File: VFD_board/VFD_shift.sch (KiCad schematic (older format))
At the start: 2 parts

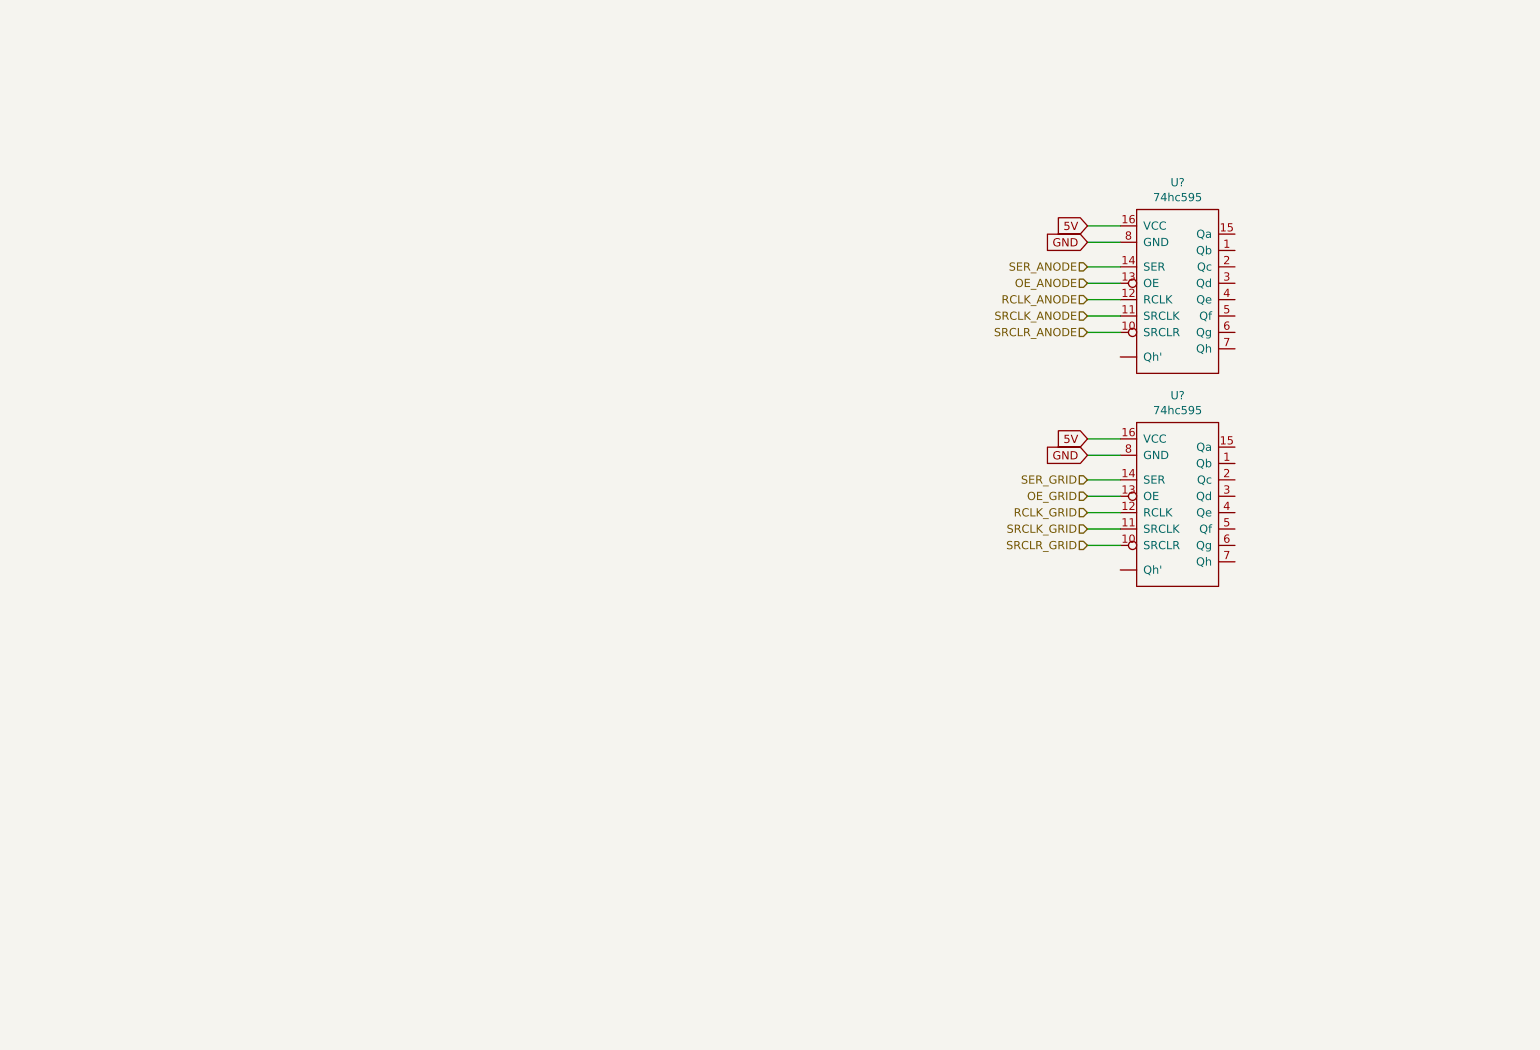
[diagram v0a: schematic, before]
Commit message: Started schematic for shift registers/drivers
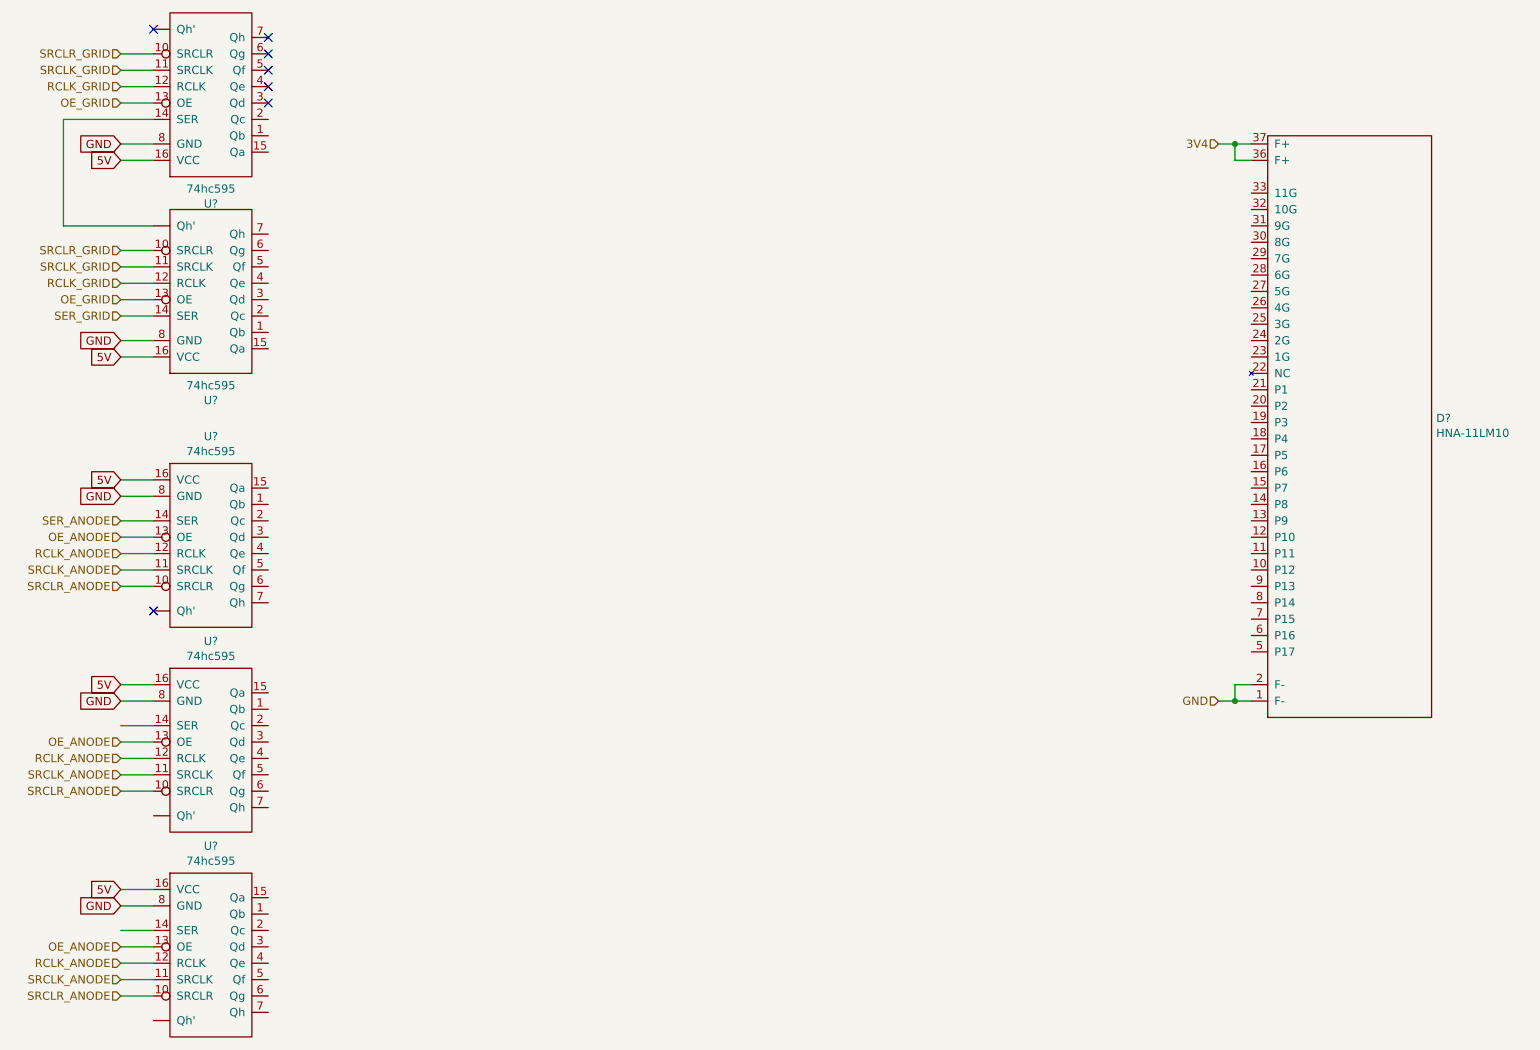
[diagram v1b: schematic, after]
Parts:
- added D?: HNA-11LM10, symbol bambouLab:HNA-11LM10
- added U? (x3): 74hc595, symbol bambouLab:74hc595
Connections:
- net labels added: 3V4
- wire segments 14 -> 45
- no-connect marks 0 -> 7
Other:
- moved on the sheet: U?
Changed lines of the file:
@@
 L bambouLab:74hc595 U?
 U 1 1 5EC463A4
-P 8950 3500
-F 0 "U?" H 8950 3915 50  0000 C CNN
-F 1 "74hc595" H 8950 3824 50  0000 C CNN
-F 2 "" H 8650 3500 50  0001 C CNN
-F 3 "" H 8650 3500 50  0001 C CNN
-	1    8950 3500
+P 3050 2700
+F 0 "U?" H 3050 3115 50  0000 C CNN
+F 1 "74hc595" H 3050 3024 50  0000 C CNN
+F 2 "" H 2750 2700 50  0001 C CNN
+F 3 "" H 2750 2700 50  0001 C CNN
+	1    3050 2700
+	1    0    0    1
+$EndComp
+Text GLabel 2500 2850 0    50   Input ~ 0
+5V
+Text GLabel 2500 2750 0    50   Input ~ 0
+GND
+Wire Wire Line
+	2500 2850 2700 2850
+Wire Wire Line
+	2700 2750 2500 2750
+Wire Wire Line
+	2500 2600 2700 2600
+Wire Wire Line
+	2500 2500 2700 2500
+Wire Wire Line
+	2500 2400 2700 2400
+Wire Wire Line
+	2500 2300 2700 2300
+Wire Wire Line
+	2500 2200 2700 2200
+$Comp
+L bambouLab:74hc595 U?
+U 1 1 5EC4864B
+P 3050 6250
+F 0 "U?" H 3050 6665 50  0000 C CNN
+F 1 "74hc595" H 3050 6574 50  0000 C CNN
+F 2 "" H 2750 6250 50  0001 C CNN
+F 3 "" H 2750 6250 50  0001 C CNN
+	1    3050 6250
 	1    0    0    -1
 $EndComp
-Text GLabel 8400 3350 0    50   Input ~ 0
-5V
-Text GLabel 8400 3450 0    50   Input ~ 0
-GND
-Wire Wire Line
-	8400 3350 8600 3350
-Wire Wire Line
-	8600 3450 8400 3450
-Wire Wire Line
-	8400 3600 8600 3600
-Wire Wire Line
-	8400 3700 8600 3700
-Wire Wire Line
-	8400 3800 8600 3800
-Wire Wire Line
-	8400 3900 8600 3900
-Wire Wire Line
-	8400 4000 8600 4000
-$Comp
-L bambouLab:74hc595 U?
-U 1 1 5EC4864B
-P 8950 2200
-F 0 "U?" H 8950 2615 50  0000 C CNN
-F 1 "74hc595" H 8950 2524 50  0000 C CNN
-F 2 "" H 8650 2200 50  0001 C CNN
-F 3 "" H 8650 2200 50  0001 C CNN
-	1    8950 2200
+Text GLabel 2500 6100 0    50   Input ~ 0
+5V
+Text GLabel 2500 6200 0    50   Input ~ 0
+GND
+Wire Wire Line
+	2500 6100 2700 6100
+Wire Wire Line
+	2700 6200 2500 6200
+Wire Wire Line
+	2500 6350 2700 6350
+Wire Wire Line
+	2500 6450 2700 6450
+Wire Wire Line
+	2500 6550 2700 6550
+Wire Wire Line
+	2500 6650 2700 6650
+Wire Wire Line
+	2500 6750 2700 6750
+Text HLabel 2500 3850 0    50   Input ~ 0
+SER_ANODE
+Text HLabel 2500 6450 0    50   Input ~ 0
+OE_ANODE
+Text HLabel 2500 6550 0    50   Input ~ 0
+RCLK_ANODE
+Text HLabel 2500 6650 0    50   Input ~ 0
+SRCLK_ANODE
+Text HLabel 2500 6750 0    50   Input ~ 0
+SRCLR_ANODE
+Text HLabel 2500 2600 0    50   Input ~ 0
+SER_GRID
+Text HLabel 2500 2500 0    50   Input ~ 0
+OE_GRID
+Text HLabel 2500 2400 0    50   Input ~ 0
+RCLK_GRID
+Text HLabel 2500 2300 0    50   Input ~ 0
+SRCLK_GRID
+Text HLabel 2500 2200 0    50   Input ~ 0
+SRCLR_GRID
+$Comp
+L bambouLab:HNA-11LM10 D?
+U 1 1 5EC5CCB5
+P 9500 3350
+F 0 "D?" H 8472 3476 50  0000 R CNN
+F 1 "HNA-11LM10" H 8472 3385 50  0000 R CNN
+F 2 "" H 9600 5450 50  0001 C CNN
+F 3 "" H 9600 5450 50  0001 C CNN
+	1    9500 3350
+	-1   0    0    -1
+$EndComp
+Text HLabel 9200 1550 0    50   Input ~ 0
+3V4
+Wire Wire Line
+	9200 1550 9300 1550
+Wire Wire Line
+	9400 1650 9300 1650
+Wire Wire Line
+	9300 1650 9300 1550
+Connection ~ 9300 1550
+Wire Wire Line
+	9300 1550 9400 1550
+Text HLabel 9200 4950 0    50   Input ~ 0
+GND
+Wire Wire Line
+	9400 4950 9300 4950
+Wire Wire Line
+	9300 4950 9300 4850
+Wire Wire Line
+	9300 4850 9400 4850
+Wire Wire Line
+	9300 4950 9200 4950
+Connection ~ 9300 4950
+$Comp
+L bambouLab:74hc595 U?
+U 1 1 5EC661E6
+P 3050 1500
+F 0 "U?" H 3050 1915 50  0000 C CNN
+F 1 "74hc595" H 3050 1824 50  0000 C CNN
+F 2 "" H 2750 1500 50  0001 C CNN
+F 3 "" H 2750 1500 50  0001 C CNN
+	1    3050 1500
+	1    0    0    1
+$EndComp
+Text GLabel 2500 1650 0    50   Input ~ 0
+5V
+Text GLabel 2500 1550 0    50   Input ~ 0
+GND
+Wire Wire Line
+	2500 1650 2700 1650
+Wire Wire Line
+	2700 1550 2500 1550
+Wire Wire Line
+	2500 1300 2700 1300
+Wire Wire Line
+	2500 1200 2700 1200
+Wire Wire Line
+	2500 1100 2700 1100
+Wire Wire Line
+	2500 1000 2700 1000
+Text HLabel 2500 1300 0    50   Input ~ 0
+OE_GRID
+Text HLabel 2500 1200 0    50   Input ~ 0
+RCLK_GRID
+Text HLabel 2500 1100 0    50   Input ~ 0
+SRCLK_GRID
+Text HLabel 2500 1000 0    50   Input ~ 0
+SRCLR_GRID
+Wire Wire Line
+	2150 2050 2700 2050
+Wire Wire Line
+	2150 1400 2700 1400
+$Comp
+L bambouLab:74hc595 U?
+U 1 1 5EC76158
+P 3050 3750
+F 0 "U?" H 3050 4165 50  0000 C CNN
+F 1 "74hc595" H 3050 4074 50  0000 C CNN
+F 2 "" H 2750 3750 50  0001 C CNN
+F 3 "" H 2750 3750 50  0001 C CNN
+	1    3050 3750
 	1    0    0    -1
 $EndComp
-Text GLabel 8400 2050 0    50   Input ~ 0
-5V
-Text GLabel 8400 2150 0    50   Input ~ 0
-GND
-Wire Wire Line
-	8400 2050 8600 2050
-Wire Wire Line
-	8600 2150 8400 2150
-Wire Wire Line
-	8400 2300 8600 2300
-Wire Wire Line
-	8400 2400 8600 2400
-Wire Wire Line
-	8400 2500 8600 2500
-Wire Wire Line
-	8400 2600 8600 2600
-Wire Wire Line
-	8400 2700 8600 2700
-Text HLabel 8400 2300 0    50   Input ~ 0
-SER_ANODE
-Text HLabel 8400 2400 0    50   Input ~ 0
+$Comp
+L bambouLab:74hc595 U?
+U 1 1 5EC7615E
+P 3050 5000
+F 0 "U?" H 3050 5415 50  0000 C CNN
+F 1 "74hc595" H 3050 5324 50  0000 C CNN
+F 2 "" H 2750 5000 50  0001 C CNN
+F 3 "" H 2750 5000 50  0001 C CNN
+	1    3050 5000
+	1    0    0    -1
+$EndComp
+Wire Wire Line
+	2150 2050 2150 1400
+Text GLabel 2500 4850 0    50   Input ~ 0
+5V
+Text GLabel 2500 4950 0    50   Input ~ 0
+GND
+Wire Wire Line
+	2500 4850 2700 4850
+Wire Wire Line
+	2700 4950 2500 4950
+Wire Wire Line
+	2500 5100 2700 5100
+Wire Wire Line
+	2500 5200 2700 5200
+Wire Wire Line
+	2500 5300 2700 5300
+Wire Wire Line
+	2500 5400 2700 5400
+Wire Wire Line
+	2500 5500 2700 5500
+Text HLabel 2500 5200 0    50   Input ~ 0
 OE_ANODE
-Text HLabel 8400 2500 0    50   Input ~ 0
+Text HLabel 2500 5300 0    50   Input ~ 0
 RCLK_ANODE
-Text HLabel 8400 2600 0    50   Input ~ 0
+Text GLabel 2500 3600 0    50   Input ~ 0
+5V
+Text GLabel 2500 3700 0    50   Input ~ 0
+GND
+Wire Wire Line
+	2500 3600 2700 3600
+Wire Wire Line
+	2700 3700 2500 3700
+Wire Wire Line
+	2500 3950 2700 3950
+Wire Wire Line
+	2500 4050 2700 4050
+Wire Wire Line
+	2500 4150 2700 4150
+Wire Wire Line
+	2500 4250 2700 4250
+Text HLabel 2500 3950 0    50   Input ~ 0
+OE_ANODE
+Text HLabel 2500 4050 0    50   Input ~ 0
+RCLK_ANODE
+Wire Wire Line
+	2500 3850 2700 3850
+Text HLabel 2500 5400 0    50   Input ~ 0
 SRCLK_ANODE
-Text HLabel 8400 2700 0    50   Input ~ 0
+Text HLabel 2500 5500 0    50   Input ~ 0
 SRCLR_ANODE
-Text HLabel 8400 3600 0    50   Input ~ 0
-SER_GRID
-Text HLabel 8400 3700 0    50   Input ~ 0
-OE_GRID
-Text HLabel 8400 3800 0    50   Input ~ 0
-RCLK_GRID
-Text HLabel 8400 3900 0    50   Input ~ 0
-SRCLK_GRID
-Text HLabel 8400 4000 0    50   Input ~ 0
-SRCLR_GRID
+Text HLabel 2500 4150 0    50   Input ~ 0
+SRCLK_ANODE
+Text HLabel 2500 4250 0    50   Input ~ 0
+SRCLR_ANODE
+NoConn ~ 2700 4400
+NoConn ~ 3400 1300
+NoConn ~ 3400 1200
+NoConn ~ 3400 1100
+NoConn ~ 3400 1000
+NoConn ~ 3400 900
+NoConn ~ 2700 850
 $EndSCHEMATC
